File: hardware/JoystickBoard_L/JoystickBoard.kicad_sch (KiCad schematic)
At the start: 8 parts, among them J1 RJHSE-3380, J2 S1, J3 S2, J4 JoyX, J5 JoyY, J6 LED1, J7 LED2

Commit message: Updates to Joystick_L
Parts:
- J2, J3, J6, J7: footprint Connector_PinHeader_2.54mm:PinHeader_1x02_P2.54mm_Vertical -> Connector_JST:JST_XH_B2B-XH-A_1x02_P2.50mm_Vertical
- J4, J5: footprint Connector_PinHeader_2.54mm:PinHeader_1x03_P2.54mm_Vertical -> Useful Modifications:Analog_joystick_pot
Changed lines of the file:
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@@
       (effects (font (size 1.27 1.27)))
     )
-    (property "Footprint" "Connector_PinHeader_2.54mm:PinHeader_1x03_P2.54mm_Vertical" (at 168.91 93.98 0)
+    (property "Footprint" "Useful Modifications:Analog_joystick_pot" (at 168.91 93.98 0)
       (effects (font (size 1.27 1.27)) hide)
     )
@@
       (effects (font (size 1.27 1.27)))
     )
-    (property "Footprint" "Connector_PinHeader_2.54mm:PinHeader_1x02_P2.54mm_Vertical" (at 196.85 57.15 0)
+    (property "Footprint" "Connector_JST:JST_XH_B2B-XH-A_1x02_P2.50mm_Vertical" (at 196.85 57.15 0)
       (effects (font (size 1.27 1.27)) hide)
     )
@@
       (effects (font (size 1.27 1.27)))
     )
-    (property "Footprint" "Connector_PinHeader_2.54mm:PinHeader_1x02_P2.54mm_Vertical" (at 168.91 57.15 0)
+    (property "Footprint" "Connector_JST:JST_XH_B2B-XH-A_1x02_P2.50mm_Vertical" (at 168.91 57.15 0)
       (effects (font (size 1.27 1.27)) hide)
     )
@@
       (effects (font (size 1.27 1.27)))
     )
-    (property "Footprint" "Connector_PinHeader_2.54mm:PinHeader_1x02_P2.54mm_Vertical" (at 167.64 67.31 0)
+    (property "Footprint" "Connector_JST:JST_XH_B2B-XH-A_1x02_P2.50mm_Vertical" (at 167.64 67.31 0)
       (effects (font (size 1.27 1.27)) hide)
     )
@@
       (effects (font (size 1.27 1.27)))
     )
-    (property "Footprint" "Connector_PinHeader_2.54mm:PinHeader_1x03_P2.54mm_Vertical" (at 168.91 81.28 0)
+    (property "Footprint" "Useful Modifications:Analog_joystick_pot" (at 168.91 81.28 0)
       (effects (font (size 1.27 1.27)) hide)
     )
@@
       (effects (font (size 1.27 1.27)))
     )
-    (property "Footprint" "Connector_PinHeader_2.54mm:PinHeader_1x02_P2.54mm_Vertical" (at 198.12 69.85 0)
-      (effects (font (size 1.27 1.27)) hide)
-    )
+    (property "Footprint" "Connector_JST:JST_XH_B2B-XH-A_1x02_P2.50mm_Vertical" (at 198.12 69.85 0)
+      (effects (font (size 1.27 1.27)) hide)
+    )

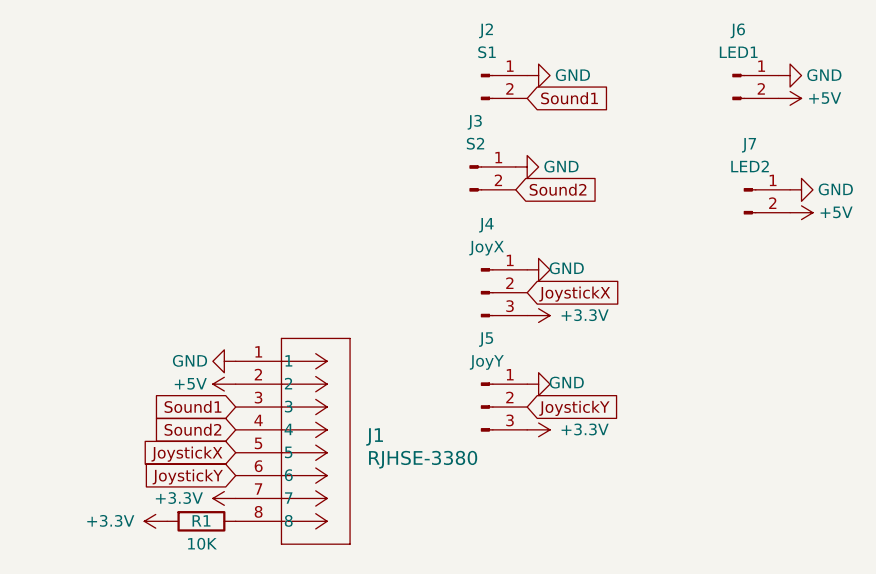
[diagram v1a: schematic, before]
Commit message: reworking L-shaped analog joystick PCB
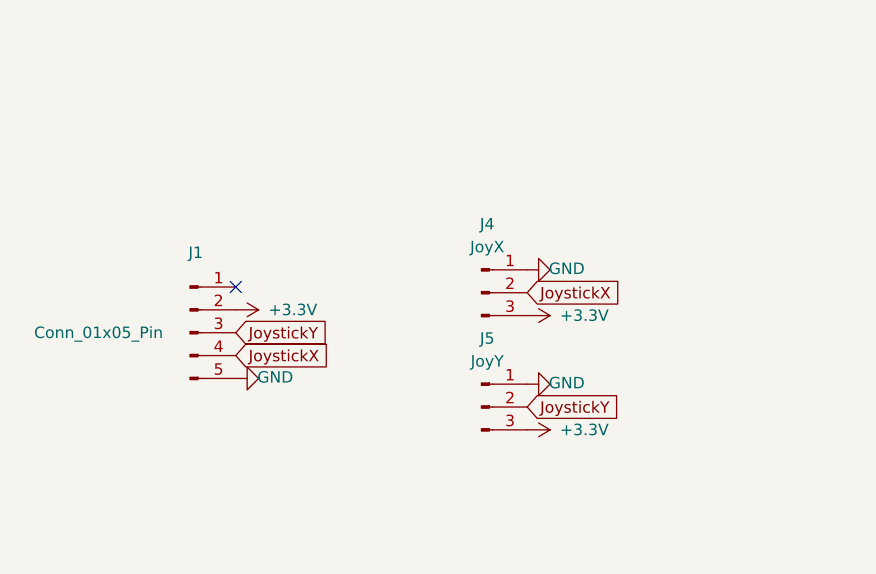
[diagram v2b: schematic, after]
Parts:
- removed J1: RJHSE-3380, Useful Modifications:CONN_RJHSE-3380_AMP, symbol RJ45_Vertical:RJHSE-3380
- removed J2: S1, Connector_JST:JST_XH_B2B-XH-A_1x02_P2.50mm_Vertical, symbol Connector:Conn_01x02_Pin
- removed J3: S2, Connector_JST:JST_XH_B2B-XH-A_1x02_P2.50mm_Vertical, symbol Connector:Conn_01x02_Pin
- removed J6: LED1, Connector_JST:JST_XH_B2B-XH-A_1x02_P2.50mm_Vertical, symbol Connector:Conn_01x02_Pin
- removed J7: LED2, Connector_JST:JST_XH_B2B-XH-A_1x02_P2.50mm_Vertical, symbol Connector:Conn_01x02_Pin
- removed R1: 10K, Resistor_SMD:R_0805_2012Metric_Pad1.20x1.40mm_HandSolder, symbol Device:R
- added J1: Conn_01x05_Pin, Connector_JST:JST_XH_B5B-XH-A_1x05_P2.50mm_Vertical, symbol Connector:Conn_01x05_Pin
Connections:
- net +3.3V: now also J1.2 (Pin_2)
- net GND: now also J1.5 (Pin_5)
- net JoystickX: now also J1.4 (Pin_4)
- net JoystickY: now also J1.3 (Pin_3)
- no-connect marks 0 -> 1

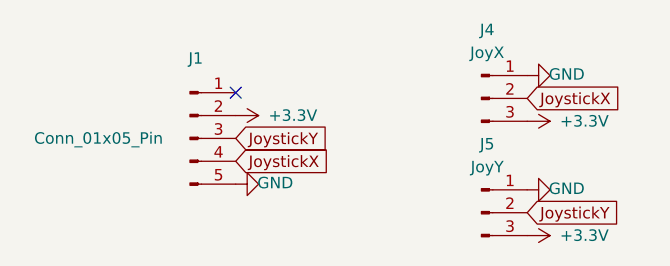
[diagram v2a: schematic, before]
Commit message: joystick L board updates
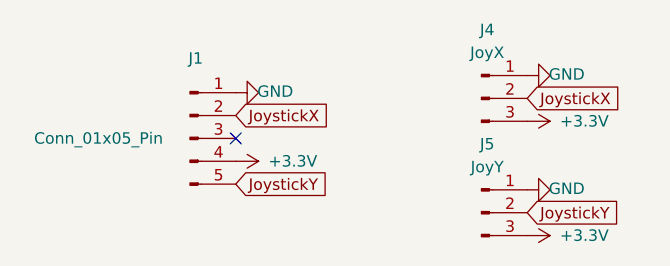
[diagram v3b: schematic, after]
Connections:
- net +3.3V: now also J1.4 (Pin_4); no longer J1.2 (Pin_2)
- net GND: now also J1.1 (Pin_1); no longer J1.5 (Pin_5)
- net JoystickX: now also J1.2 (Pin_2); no longer J1.4 (Pin_4)
- net JoystickY: now also J1.5 (Pin_5); no longer J1.3 (Pin_3)
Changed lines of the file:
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@@
 (kicad_sch (version 20230121) (generator eeschema)
   (paper "A4")
-  (no_connect (at 141.605 80.645))
+  (no_connect (at 141.605 85.725))
   (global_label "JoystickY" (shape input) (at 173.99 93.98 0) (fields_autoplaced)
     (effects (font (size 1.27 1.27)) (justify left))
@@
     )
   )
-  (global_label "JoystickY" (shape input) (at 141.605 85.725 0) (fields_autoplaced)
-    (effects (font (size 1.27 1.27)) (justify left))
-    (property "Intersheetrefs" "${INTERSHEET_REFS}" (at 152.5047 85.725 0)
+  (global_label "JoystickY" (shape input) (at 141.605 90.805 0) (fields_autoplaced)
+    (effects (font (size 1.27 1.27)) (justify left))
+    (property "Intersheetrefs" "${INTERSHEET_REFS}" (at 152.5047 90.805 0)
       (effects (font (size 1.27 1.27)) (justify left) hide)
     )
@@
     )
   )
-  (global_label "JoystickX" (shape input) (at 141.605 88.265 0) (fields_autoplaced)
-    (effects (font (size 1.27 1.27)) (justify left))
-    (property "Intersheetrefs" "${INTERSHEET_REFS}" (at 152.6256 88.265 0)
+  (global_label "JoystickX" (shape input) (at 141.605 83.185 0) (fields_autoplaced)
+    (effects (font (size 1.27 1.27)) (justify left))
+    (property "Intersheetrefs" "${INTERSHEET_REFS}" (at 152.6256 83.185 0)
       (effects (font (size 1.27 1.27)) (justify left) hide)
     )
@@
     )
   )
-  (symbol (lib_id "power:+3.3V") (at 141.605 83.185 270) (unit 1)
-    (in_bom yes) (on_board yes) (dnp no)
-    (property "Reference" "#PWR03" (at 137.795 83.185 0)
-      (effects (font (size 1.27 1.27)) hide)
-    )
-    (property "Value" "+3.3V" (at 147.955 83.185 90)
-      (effects (font (size 1.27 1.27)))
-    )
-    (property "Footprint" "" (at 141.605 83.185 0)
-      (effects (font (size 1.27 1.27)) hide)
-    )
-    (property "Datasheet" "" (at 141.605 83.185 0)
+  (symbol (lib_id "power:+3.3V") (at 141.605 88.265 270) (unit 1)
+    (in_bom yes) (on_board yes) (dnp no)
+    (property "Reference" "#PWR03" (at 137.795 88.265 0)
+      (effects (font (size 1.27 1.27)) hide)
+    )
+    (property "Value" "+3.3V" (at 147.955 88.265 90)
+      (effects (font (size 1.27 1.27)))
+    )
+    (property "Footprint" "" (at 141.605 88.265 0)
+      (effects (font (size 1.27 1.27)) hide)
+    )
+    (property "Datasheet" "" (at 141.605 88.265 0)
       (effects (font (size 1.27 1.27)) hide)
     )
@@
     )
   )
-  (symbol (lib_id "power:GND") (at 141.605 90.805 90) (unit 1)
-    (in_bom yes) (on_board yes) (dnp no)
-    (property "Reference" "#PWR02" (at 147.955 90.805 0)
-      (effects (font (size 1.27 1.27)) hide)
-    )
-    (property "Value" "GND" (at 145.9992 90.678 90)
-      (effects (font (size 1.27 1.27)))
-    )
-    (property "Footprint" "" (at 141.605 90.805 0)
-      (effects (font (size 1.27 1.27)) hide)
-    )
-    (property "Datasheet" "" (at 141.605 90.805 0)
-      (effects (font (size 1.27 1.27)) hide)
-    )
+  (symbol (lib_id "power:GND") (at 141.605 80.645 90) (unit 1)
+    (in_bom yes) (on_board yes) (dnp no)
+    (property "Reference" "#PWR02" (at 147.955 80.645 0)
+      (effects (font (size 1.27 1.27)) hide)
+    )
+    (property "Value" "GND" (at 145.9992 80.518 90)
+      (effects (font (size 1.27 1.27)))
+    )
+    (property "Footprint" "" (at 141.605 80.645 0)
+      (effects (font (size 1.27 1.27)) hide)
+    )
+    (property "Datasheet" "" (at 141.605 80.645 0)
+      (effects (font (size 1.27 1.27)) hide)
+    )
